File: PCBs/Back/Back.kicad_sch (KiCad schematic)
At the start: 6 parts

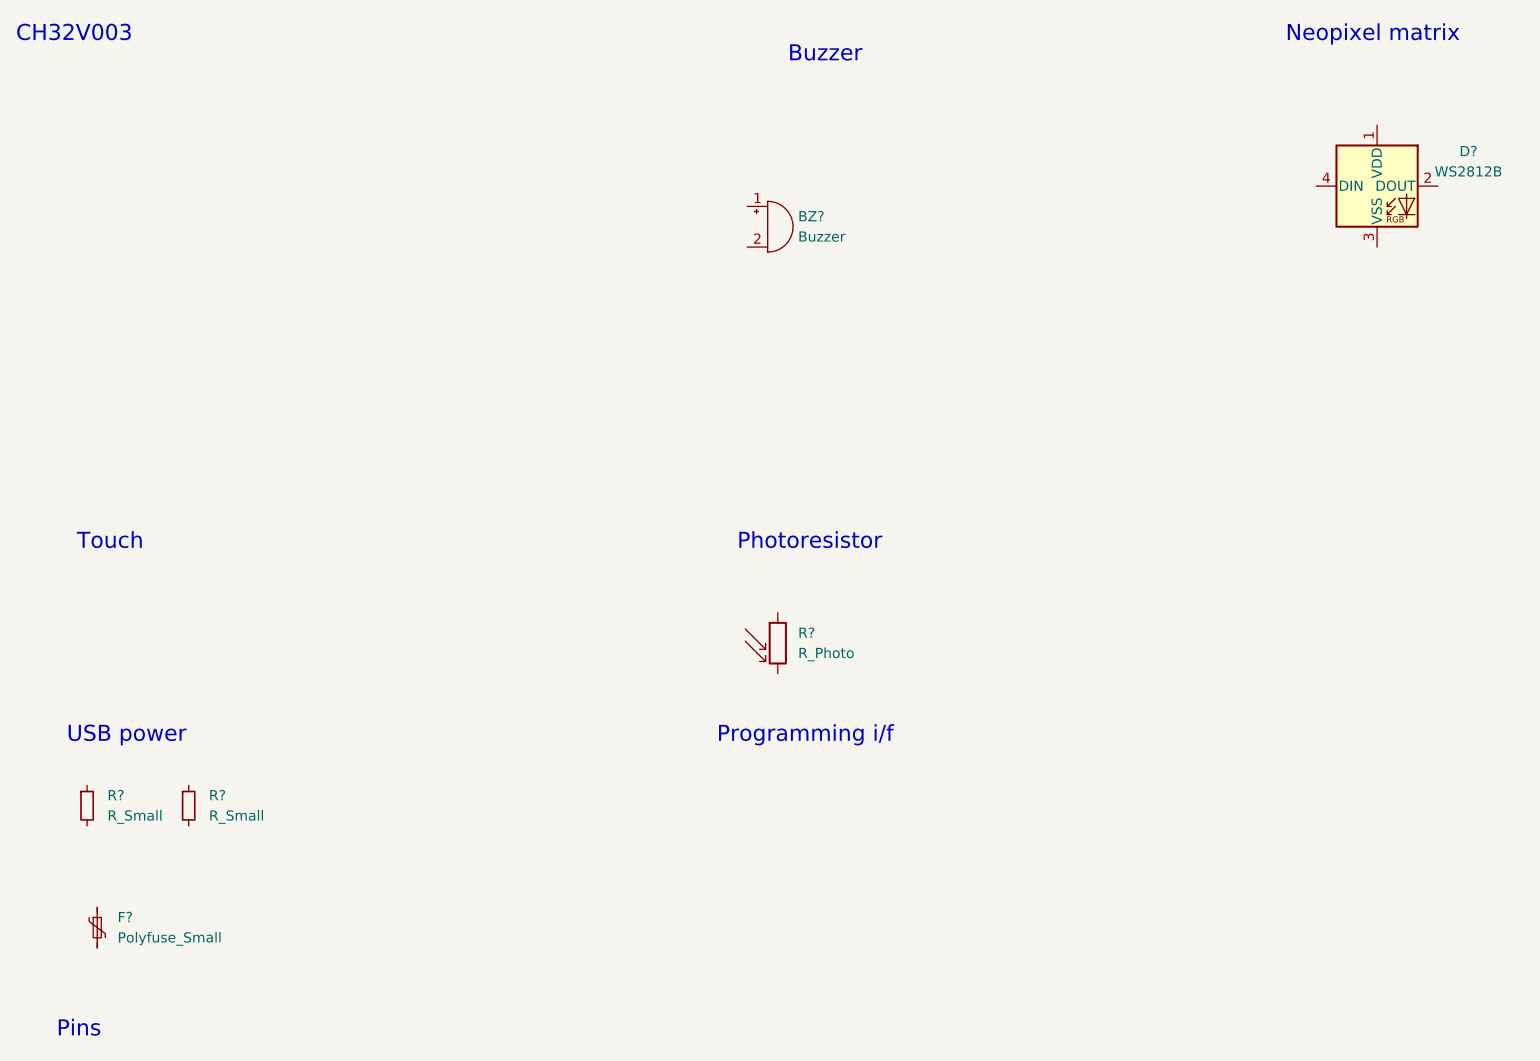
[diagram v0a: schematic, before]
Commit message: Add ch32 component
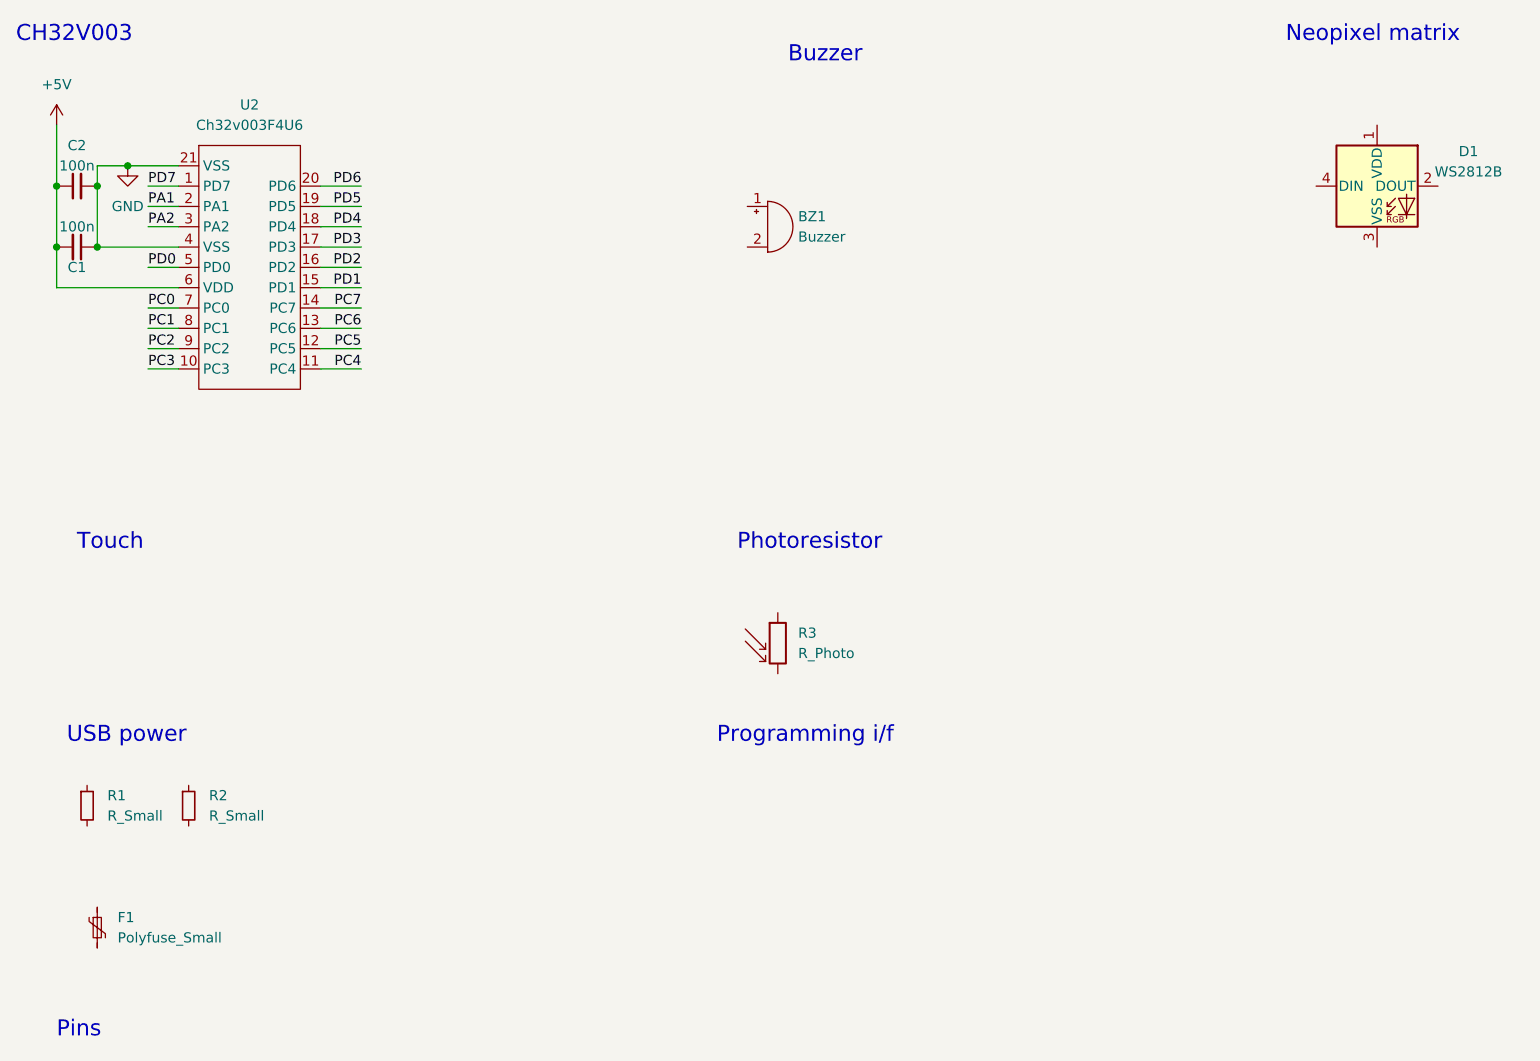
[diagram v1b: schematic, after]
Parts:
- added C1, C2: 100n, symbol Device:C_Small
- added U2: Ch32v003F4U6, Package_DFN_QFN:QFN-20-1EP_3x3mm_P0.4mm_EP1.65x1.65mm, symbol Back-lib:Ch32v003F4U6
- gave numbers to parts that had none: 6
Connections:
- new net +5V: C1.2, C2.1, U2.6 (VDD)
- new net GND: C1.1, C2.2, U2.21 (VSS), U2.4 (VSS)
- new net PA1: U2.2 (PA1)
- new net PA2: U2.3 (PA2)
- new net PC0: U2.7 (PC0)
- new net PC1: U2.8 (PC1)
- new net PC2: U2.9 (PC2)
- new net PC3: U2.10 (PC3)
- new net PC4: U2.11 (PC4)
- new net PC5: U2.12 (PC5)
- new net PC6: U2.13 (PC6)
- new net PC7: U2.14 (PC7)
- new net PD0: U2.5 (PD0)
- new net PD1: U2.15 (PD1)
- new net PD2: U2.16 (PD2)
- new net PD3: U2.17 (PD3)
- new net PD4: U2.18 (PD4)
- new net PD5: U2.19 (PD5)
- new net PD6: U2.20 (PD6)
- new net PD7: U2.1 (PD7)

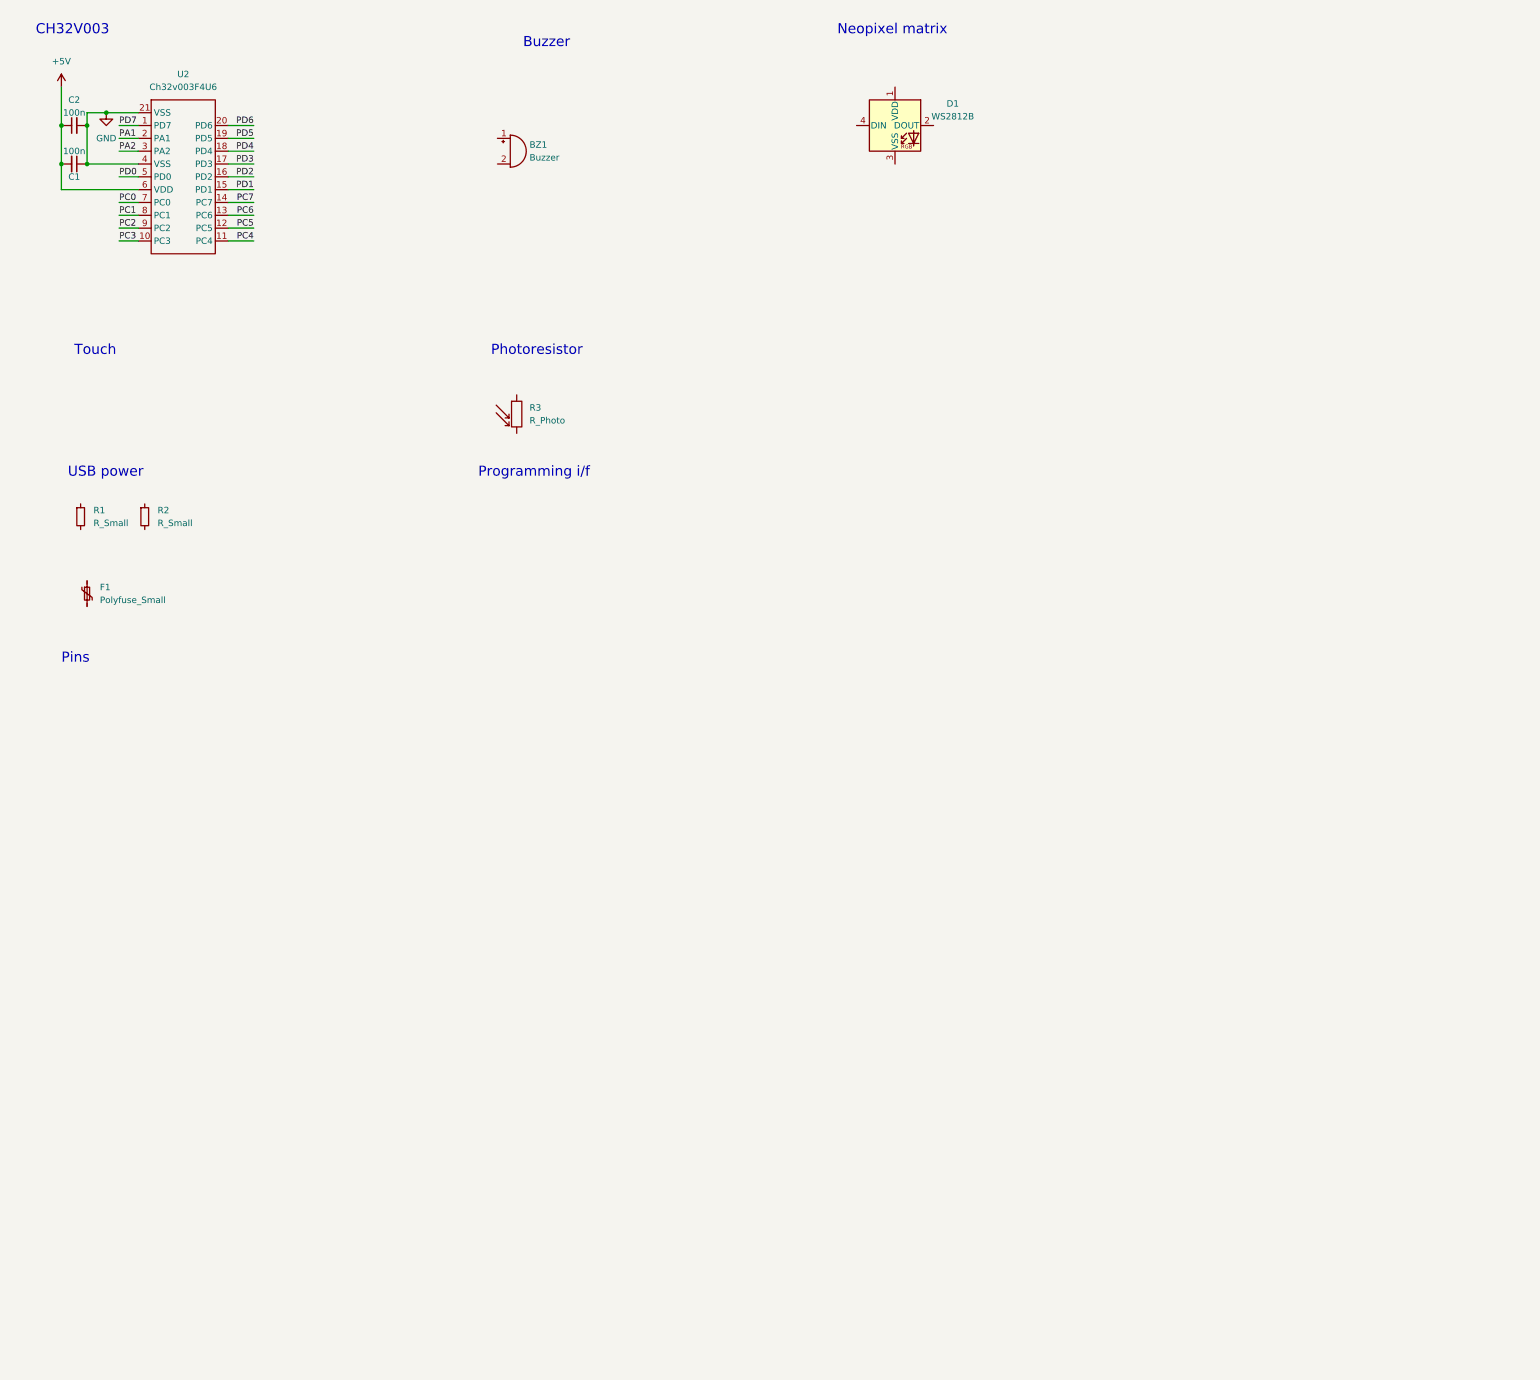
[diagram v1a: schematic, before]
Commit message: Added WS2812b
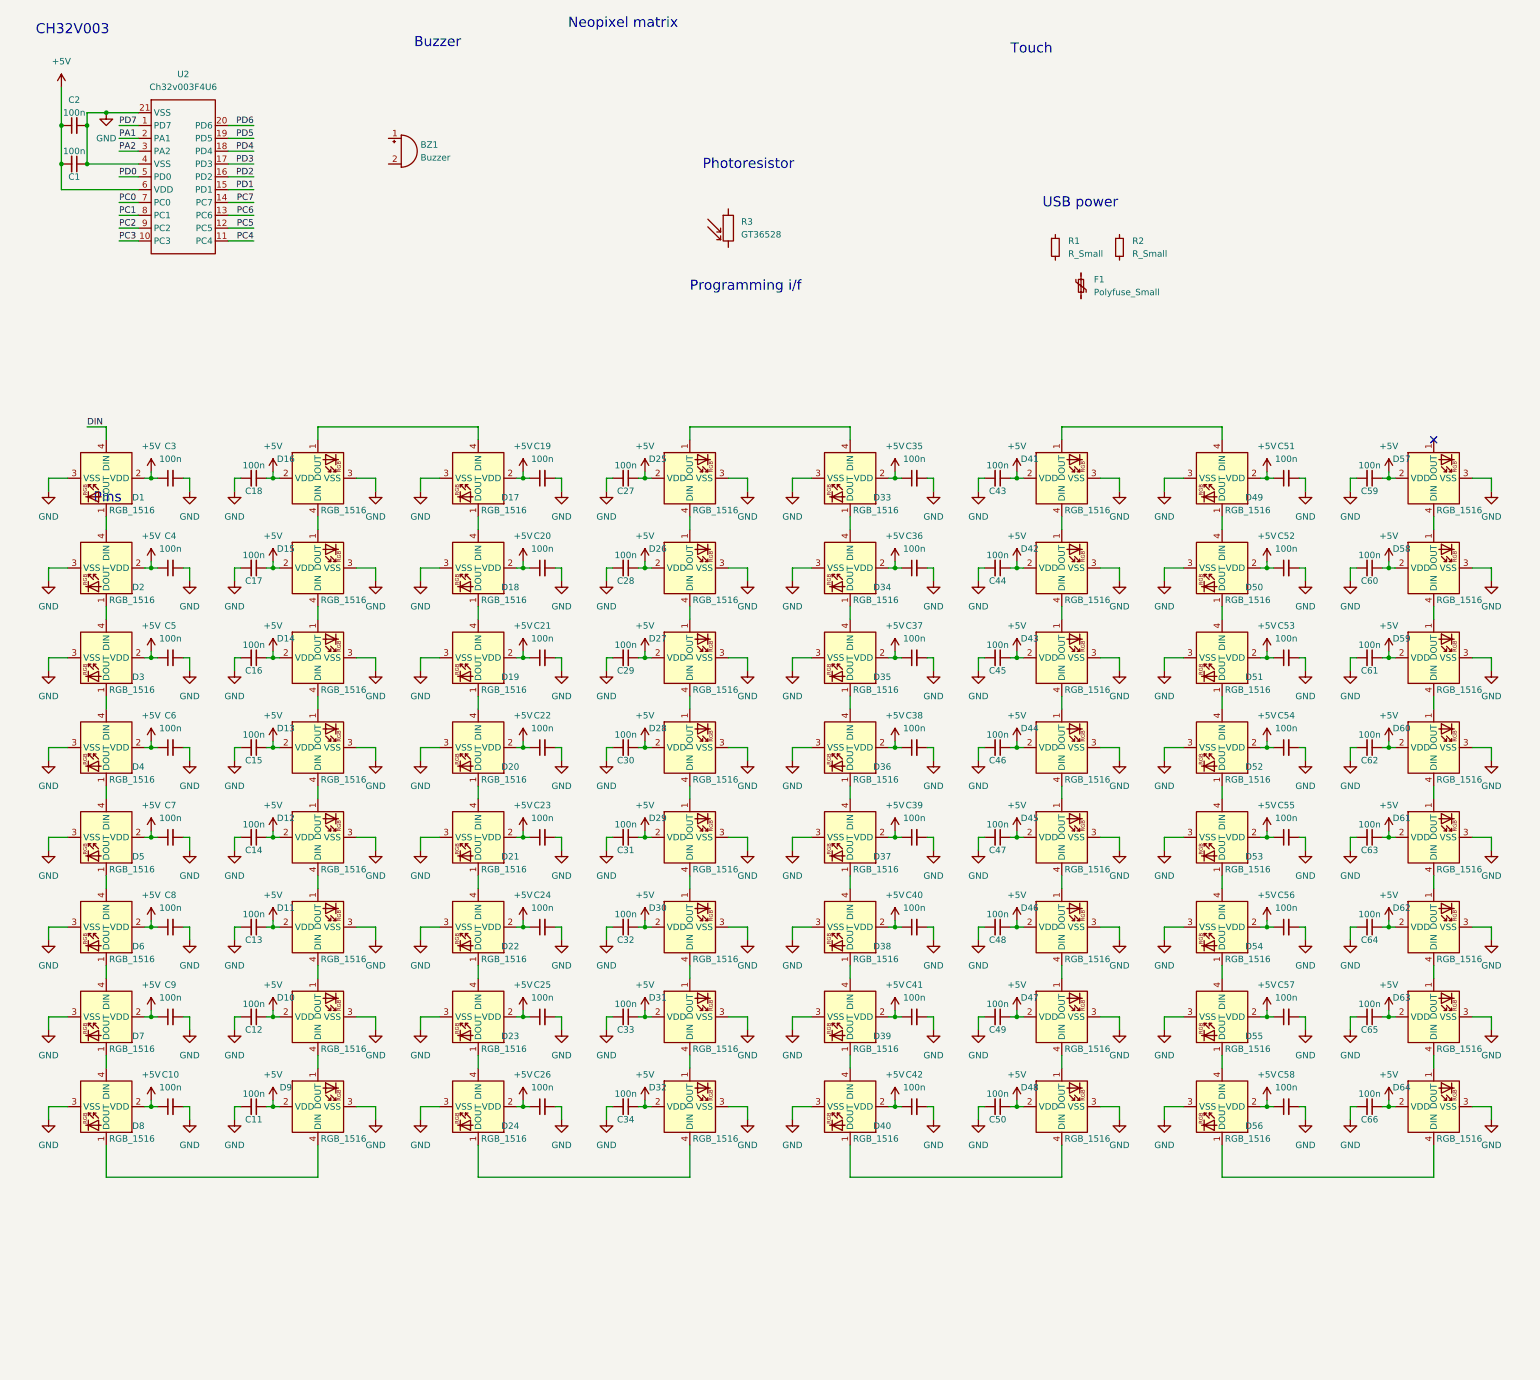
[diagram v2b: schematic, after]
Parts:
- removed D1: WS2812B, symbol LED:WS2812B
- added C10, C11, C12, C13, C14, C15, C16, C17, C18, C19, C20, C21, C22, C23, C24, C25, C26, C27, C28, C29, C3, C30, C31, C32, C33, C34, C35, C36, C37, C38, C39, C4, C40, C41, C42, C43, C44, C45, C46, C47, C48, C49, C5, C50, C51, C52, C53, C54, C55, C56, C57, C58, C59, C6, C60, C61, C62, C63, C64, C65, C66, C7, C8, C9: 100n, symbol Device:C_Small
- added D1, D10, D11, D12, D13, D14, D15, D16, D17, D18, D19, D2, D20, D21, D22, D23, D24, D25, D26, D27, D28, D29, D3, D30, D31, D32, D33, D34, D35, D36, D37, D38, D39, D4, D40, D41, D42, D43, D44, D45, D46, D47, D48, D49, D5, D50, D51, D52, D53, D54, D55, D56, D57, D58, D59, D6, D60, D61, D62, D63, D64, D7, D8, D9: RGB_1516, fp:WS2812B_1515, symbol Back-lib:WS2812B_1515
- R3: value R_Photo -> GT36528
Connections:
- net +5V: now also C10.1, C11.1, C12.1, C13.1, C14.1, C15.1, C16.1, C17.1, C18.1, C19.1, C20.1, C21.1, C22.1, C23.1, C24.1, C25.1, C26.1, C27.1, C28.1, C29.1, C3.1, C30.1, C31.1, C32.1, C33.1, C34.1, C35.1, C36.1, C37.1, C38.1, C39.1, C4.1, C40.1, C41.1, C42.1, C43.1, C44.1, C45.1, C46.1, C47.1, C48.1, C49.1, C5.1, C50.1, C51.1, C52.1, C53.1, C54.1, C55.1, C56.1, C57.1, C58.1, C59.1, C6.1, C60.1, C61.1, C62.1, C63.1, C64.1, C65.1, C66.1, C7.1, C8.1, C9.1, D1.2 (VDD), D10.2 (VDD), D11.2 (VDD), D12.2 (VDD), D13.2 (VDD), D14.2 (VDD), D15.2 (VDD), D16.2 (VDD), D17.2 (VDD), D18.2 (VDD), D19.2 (VDD), D2.2 (VDD), D20.2 (VDD), D21.2 (VDD), D22.2 (VDD), D23.2 (VDD), D24.2 (VDD), D25.2 (VDD), D26.2 (VDD), D27.2 (VDD), D28.2 (VDD), D29.2 (VDD), D3.2 (VDD), D30.2 (VDD), D31.2 (VDD), D32.2 (VDD), D33.2 (VDD), D34.2 (VDD), D35.2 (VDD), D36.2 (VDD), D37.2 (VDD), D38.2 (VDD), D39.2 (VDD), D4.2 (VDD), D40.2 (VDD), D41.2 (VDD), D42.2 (VDD), D43.2 (VDD), D44.2 (VDD), D45.2 (VDD), D46.2 (VDD), D47.2 (VDD), D48.2 (VDD), D49.2 (VDD), D5.2 (VDD), D50.2 (VDD), D51.2 (VDD), D52.2 (VDD), D53.2 (VDD), D54.2 (VDD), D55.2 (VDD), D56.2 (VDD), D57.2 (VDD), D58.2 (VDD), D59.2 (VDD), D6.2 (VDD), D60.2 (VDD), D61.2 (VDD), D62.2 (VDD), D63.2 (VDD), D64.2 (VDD), D7.2 (VDD), D8.2 (VDD), D9.2 (VDD)
- net GND: now also C10.2, C11.2, C12.2, C13.2, C14.2, C15.2, C16.2, C17.2, C18.2, C19.2, C20.2, C21.2, C22.2, C23.2, C24.2, C25.2, C26.2, C27.2, C28.2, C29.2, C3.2, C30.2, C31.2, C32.2, C33.2, C34.2, C35.2, C36.2, C37.2, C38.2, C39.2, C4.2, C40.2, C41.2, C42.2, C43.2, C44.2, C45.2, C46.2, C47.2, C48.2, C49.2, C5.2, C50.2, C51.2, C52.2, C53.2, C54.2, C55.2, C56.2, C57.2, C58.2, C59.2, C6.2, C60.2, C61.2, C62.2, C63.2, C64.2, C65.2, C66.2, C7.2, C8.2, C9.2, D1.3 (VSS), D10.3 (VSS), D11.3 (VSS), D12.3 (VSS), D13.3 (VSS), D14.3 (VSS), D15.3 (VSS), D16.3 (VSS), D17.3 (VSS), D18.3 (VSS), D19.3 (VSS), D2.3 (VSS), D20.3 (VSS), D21.3 (VSS), D22.3 (VSS), D23.3 (VSS), D24.3 (VSS), D25.3 (VSS), D26.3 (VSS), D27.3 (VSS), D28.3 (VSS), D29.3 (VSS), D3.3 (VSS), D30.3 (VSS), D31.3 (VSS), D32.3 (VSS), D33.3 (VSS), D34.3 (VSS), D35.3 (VSS), D36.3 (VSS), D37.3 (VSS), D38.3 (VSS), D39.3 (VSS), D4.3 (VSS), D40.3 (VSS), D41.3 (VSS), D42.3 (VSS), D43.3 (VSS), D44.3 (VSS), D45.3 (VSS), D46.3 (VSS), D47.3 (VSS), D48.3 (VSS), D49.3 (VSS), D5.3 (VSS), D50.3 (VSS), D51.3 (VSS), D52.3 (VSS), D53.3 (VSS), D54.3 (VSS), D55.3 (VSS), D56.3 (VSS), D57.3 (VSS), D58.3 (VSS), D59.3 (VSS), D6.3 (VSS), D60.3 (VSS), D61.3 (VSS), D62.3 (VSS), D63.3 (VSS), D64.3 (VSS), D7.3 (VSS), D8.3 (VSS), D9.3 (VSS)
- new net: D2.1 (DOUT), D3.4 (DIN)
- new net: D1.1 (DOUT), D2.4 (DIN)
- new net: D61.4 (DIN), D62.1 (DOUT)
- new net: D62.4 (DIN), D63.1 (DOUT)
- new net: D55.1 (DOUT), D56.4 (DIN)
- new net: D54.1 (DOUT), D55.4 (DIN)
- new net: D23.1 (DOUT), D24.4 (DIN)
- new net: D22.1 (DOUT), D23.4 (DIN)
- new net: D25.1 (DOUT), D33.4 (DIN)
- new net: D25.4 (DIN), D26.1 (DOUT)
- new net: D44.4 (DIN), D45.1 (DOUT)
- new net: D45.4 (DIN), D46.1 (DOUT)
- new net: D43.4 (DIN), D44.1 (DOUT)
- new net: D5.1 (DOUT), D6.4 (DIN)
- new net: D4.1 (DOUT), D5.4 (DIN)
- new net: D41.1 (DOUT), D49.4 (DIN)
- new net: D41.4 (DIN), D42.1 (DOUT)
- new net: D15.1 (DOUT), D16.4 (DIN)
- new net: D14.1 (DOUT), D15.4 (DIN)
- new net: D47.4 (DIN), D48.1 (DOUT)
- new net: D40.1 (DOUT), D48.4 (DIN)
- new net: D17.1 (DOUT), D18.4 (DIN)
- new net: D16.1 (DOUT), D17.4 (DIN)
- new net: D60.4 (DIN), D61.1 (DOUT)
- new net: D36.1 (DOUT), D37.4 (DIN)
- new net: D35.1 (DOUT), D36.4 (DIN)
- new net: D34.1 (DOUT), D35.4 (DIN)
- new net: D33.1 (DOUT), D34.4 (DIN)
- new net: D57.4 (DIN), D58.1 (DOUT)
- new net: D58.4 (DIN), D59.1 (DOUT)
- new net: D12.1 (DOUT), D13.4 (DIN)
- new net: D11.1 (DOUT), D12.4 (DIN)
- new net: D21.1 (DOUT), D22.4 (DIN)
- new net: D20.1 (DOUT), D21.4 (DIN)
- new net: D28.4 (DIN), D29.1 (DOUT)
- new net: D29.4 (DIN), D30.1 (DOUT)
- new net: D42.4 (DIN), D43.1 (DOUT)
- new net: D3.1 (DOUT), D4.4 (DIN)
- new net: D37.1 (DOUT), D38.4 (DIN)
- new net: D50.1 (DOUT), D51.4 (DIN)
- new net: D49.1 (DOUT), D50.4 (DIN)
- new net: D39.1 (DOUT), D40.4 (DIN)
- new net: D38.1 (DOUT), D39.4 (DIN)
- new net: D26.4 (DIN), D27.1 (DOUT)
- new net: D8.1 (DOUT), D9.4 (DIN)
- new net: D7.1 (DOUT), D8.4 (DIN)
- new net: D30.4 (DIN), D31.1 (DOUT)
- new net: D13.1 (DOUT), D14.4 (DIN)
- new net: D6.1 (DOUT), D7.4 (DIN)
- new net: D18.1 (DOUT), D19.4 (DIN)
- new net: D27.4 (DIN), D28.1 (DOUT)
- new net: D19.1 (DOUT), D20.4 (DIN)
- new net: D10.4 (DIN), D9.1 (DOUT)
- new net: D24.1 (DOUT), D32.4 (DIN)
- new net: D53.1 (DOUT), D54.4 (DIN)
- new net: D52.1 (DOUT), D53.4 (DIN)
- new net: D10.1 (DOUT), D11.4 (DIN)
- new net: D31.4 (DIN), D32.1 (DOUT)
- new net: D59.4 (DIN), D60.1 (DOUT)
- new net: D46.4 (DIN), D47.1 (DOUT)
- new net: D63.4 (DIN), D64.1 (DOUT)
- new net: D56.1 (DOUT), D64.4 (DIN)
- new net: D51.1 (DOUT), D52.4 (DIN)
- new net DIN: D1.4 (DIN)
- no-connect marks 0 -> 1
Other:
- moved on the sheet: BZ1, F1, R1, R2, R3

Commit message: update back schem
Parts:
- added J1: TC2030, Connector:Tag-Connect_TC2030-IDC-NL_2x03_P1.27mm_Vertical, symbol Connector:Conn_ARM_SWD_TagConnect_TC2030-NL
- F1: value Polyfuse_Small -> SMD0805B050TF
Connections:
- net +5V: now also J1.1 (VCC)
- net GND: now also J1.5 (GND)
- net PD1: now also J1.2 (SWDIO)
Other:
- note added: "C5349954"
- moved on the sheet: C1, C2
